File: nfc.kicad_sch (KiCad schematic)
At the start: 21 parts, among them U4 ST25R3918AQW, Y1 27.12MHz

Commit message: Adding some stuf
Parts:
- added AE1: Antenna_Loop, footprints:badge_antenna, symbol Device:Antenna_Loop
- added C33, C34, C35, C36, C37, C38, C39, C40, C41, C42: C, Capacitor_SMD:C_0805_2012Metric, symbol Device:C
- added L2, L3: 270nH, Inductor_SMD:L_0805_2012Metric, symbol Device:L
- added R7, R8: R, Resistor_SMD:R_0805_2012Metric, symbol Device:R
- C10, C14, C8, C9: footprint Capacitor_SMD:C_0805_2012Metric -> Capacitor_SMD:C_0603_1608Metric; MFPN CL21B105KBFNNNE -> CC0603KRX7R7BB105; Voltage 50V -> 16V
- C11, C12, C13, C17, C18, C19, C20, C25: footprint Capacitor_SMD:C_0805_2012Metric -> Capacitor_SMD:C_0603_1608Metric; MFPN CL21B103KBANNNC -> CC0603KRX7R9BB103
- C21, C22, C23, C26: footprint Capacitor_SMD:C_0805_2012Metric -> Capacitor_SMD:C_0603_1608Metric; MFPN CL21A225KBQNNNE -> CC0603KRX7R7BB225; Voltage 50V -> 16V
- C24: footprint Capacitor_SMD:C_0805_2012Metric -> Capacitor_SMD:C_0603_1608Metric; MFPN CL21B102KBCNNNC -> CC0603KRX7R9BB102
- U4: footprint Package_DFN_QFN:VQFN-32-1EP_5x5mm_P0.5mm_EP3.1x3.1mm -> Package_DFN_QFN:HVQFN-32-1EP_5x5mm_P0.5mm_EP3.1x3.1mm
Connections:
- net GND: now also C33.2, C34.1, C37.2, C38.1, C39.1, C42.2
- net at C20.1, U4.14 (VDD_DR), U4.9 (VDD_RF): now also C26.2; no longer C23.2
- net at C24.1, C25.1, U4.11 (VDD_AM): now also C23.2; no longer C26.2
- net at U4.13 (RFO1): now also L2.1
- net at U4.15 (RFO2): now also L3.1
- net at U4.22 (RFI1): now also C39.2, C40.1
- net at U4.23 (RFI2): now also C41.2, C42.1
- new net: C35.2, C37.1, C40.2, R7.1
- new net: AE1.1, R7.2
- new net: AE1.2, R8.2
- new net: C33.1, C35.1, L2.2
- new net: C34.2, C36.1, L3.2
- new net: C36.2, C38.2, C41.1, R8.1
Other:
- note added: "Cap Voltage Divider"
- note added: "EMC Filter"
- note added: "Matching Network"
- note added: "Q Factor Reduction"
- moved on the sheet: C11, C12, C13, C15, C16, C17, C18, C19, C20, C21, C24, C25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

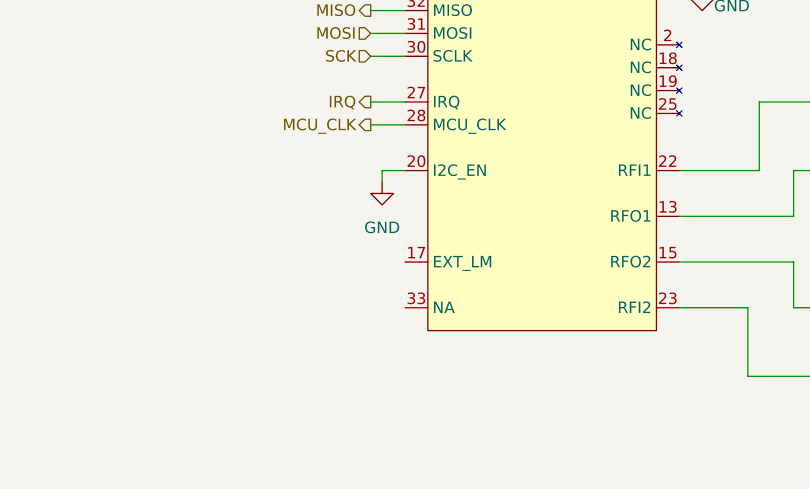
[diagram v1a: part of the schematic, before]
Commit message: Fixed most DRC errors, but need to relayout RFO/RFI
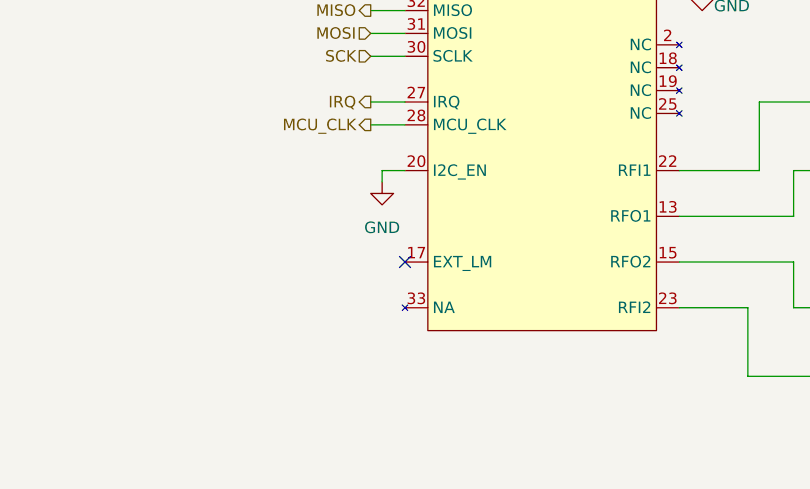
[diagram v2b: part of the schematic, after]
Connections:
- no-connect marks 0 -> 1
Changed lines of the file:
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@@
 		(color 0 0 0 0)
+	)
+	(no_connect
+		(at 106.68 121.92)
 	)
 	(wire
@@
 			)
 		)
-		(property "Datasheet" "https://www.lcsc.com/datasheet/lcsc_datasheet_2403291504_YXC-Crystal-Oscillators-X32252712MSB4SI_C70591.pdf"
+		(property "Datasheet" "~"
 			(at 96.52 82.55 0)
 			(effects

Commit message: Optimizing components for ordering
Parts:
- AE1: now left out of the parts list
- C10, C14, C8, C9: LCSC Part # (none) -> C15849; MFPN CC0603KRX7R7BB105 -> CL10A105KB8NNNC
- C11, C12, C13, C17, C18, C19, C20, C25: LCSC Part # (none) -> C57112; MFPN CC0603KRX7R9BB103 -> 0603B103K500NT
- C15, C16: LCSC Part # (none) -> C1644
- C21, C22, C23, C26: LCSC Part # (none) -> C23630; MFPN CC0603KRX7R7BB225 -> CL10A225KO8NNNC
- C24: LCSC Part # (none) -> C1588; MFPN CC0603KRX7R9BB102 -> CL10B102KB8NNNC
- L2, L3: LCSC Part # (none) -> C107522
- U4: LCSC Part # (none) -> C3304617; MFPN (none) -> ST25R3918AQW
- Y1: LCSC Part # (none) -> C70591
